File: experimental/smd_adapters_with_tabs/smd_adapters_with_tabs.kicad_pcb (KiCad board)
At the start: 2 copper layers, 79.8 x 64.6 mm, 34 parts

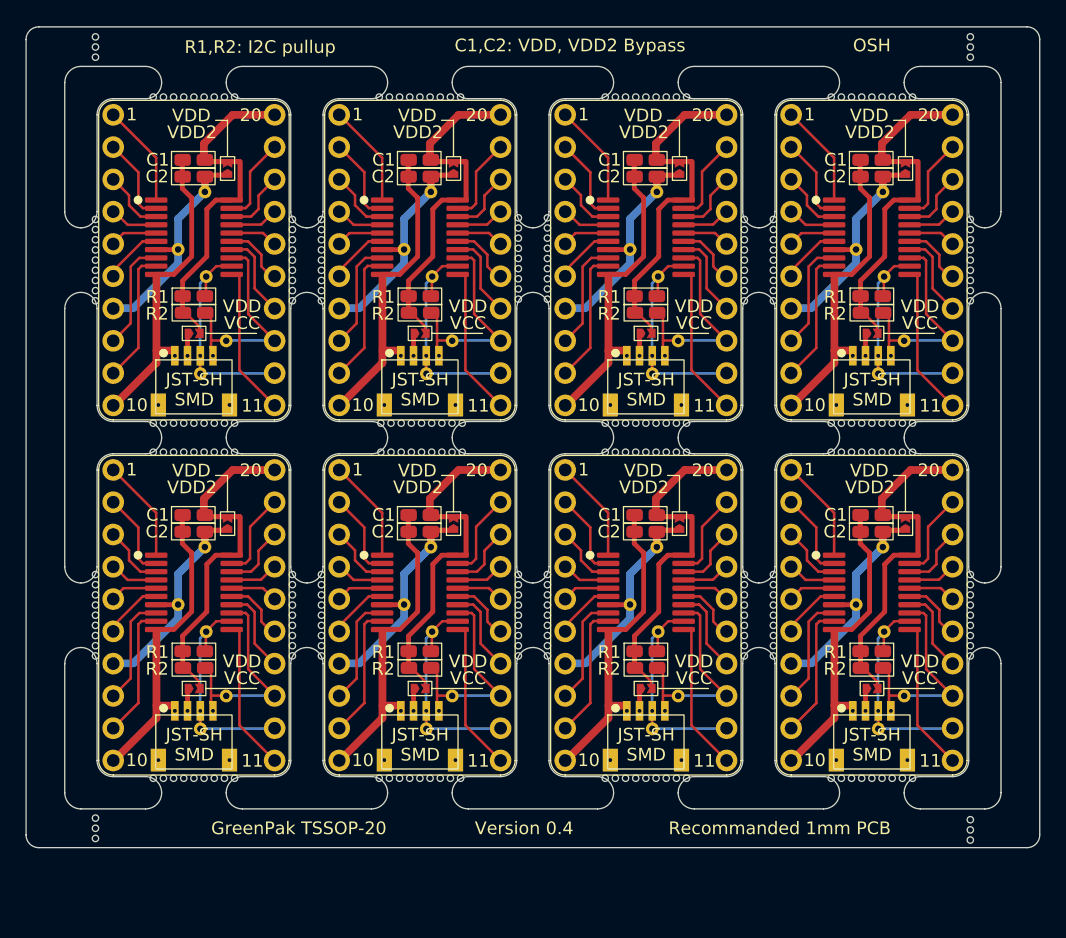
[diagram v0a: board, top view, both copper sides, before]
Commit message: Added the 24 pin footprints to the panel.
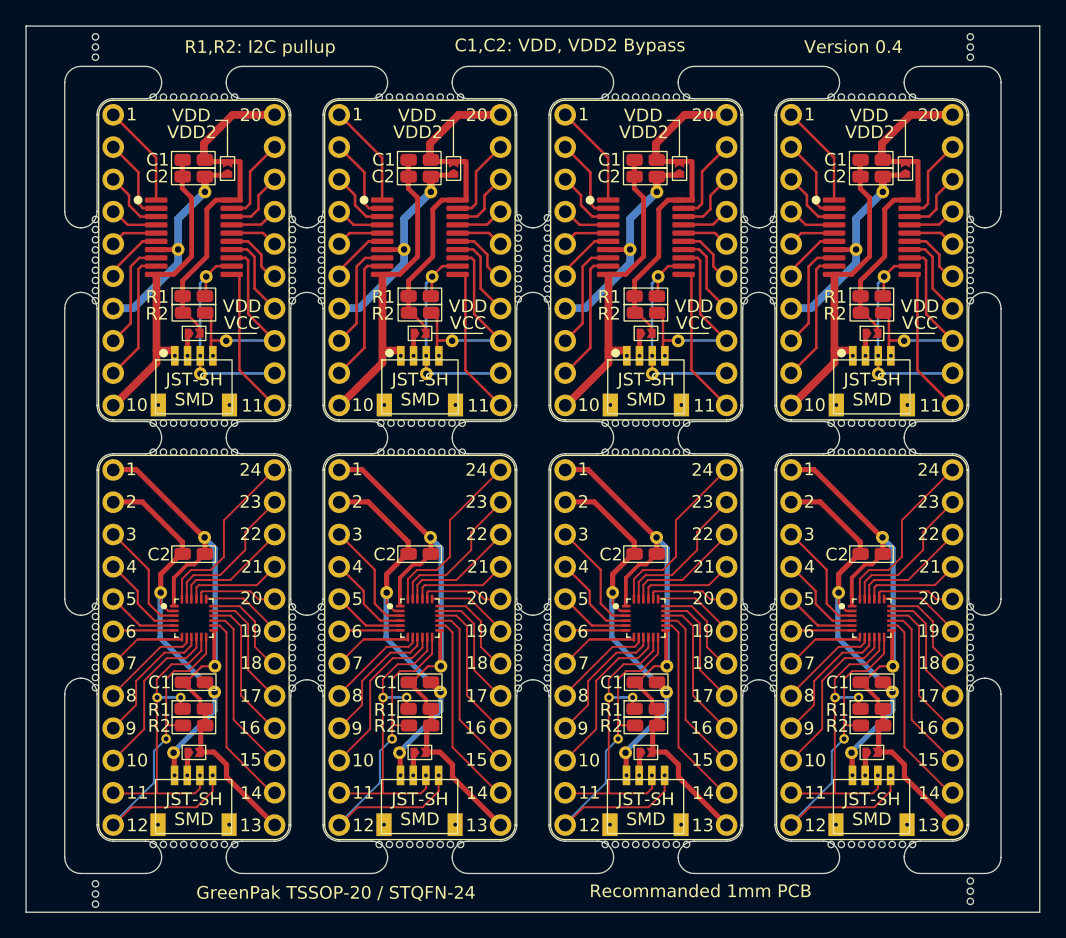
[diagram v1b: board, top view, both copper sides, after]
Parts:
- removed the REF** at (30.0, 6.86)
- removed the REF** at (-5.59, 6.86)
- removed the REF** at (-23.4, 6.86)
- removed the REF** at (12.2, 6.86)
- added REF**: GREENPAK-SMD-ADAPTER-STQFN-24-QWIIC, greenpack_smd_adapters:GREENPAK-SMD-ADAPTER-STQFN-24-QWIIC, F.Cu at (-5.59, 9.40)
- added REF**: GREENPAK-SMD-ADAPTER-STQFN-24-QWIIC, greenpack_smd_adapters:GREENPAK-SMD-ADAPTER-STQFN-24-QWIIC, F.Cu at (12.2, 9.40)
- added REF**: GREENPAK-SMD-ADAPTER-STQFN-24-QWIIC, greenpack_smd_adapters:GREENPAK-SMD-ADAPTER-STQFN-24-QWIIC, F.Cu at (-23.4, 9.40)
- added REF**: GREENPAK-SMD-ADAPTER-STQFN-24-QWIIC, greenpack_smd_adapters:GREENPAK-SMD-ADAPTER-STQFN-24-QWIIC, F.Cu at (30.0, 9.40)
- moved mouse-bite-2.54mm-slot 5.21 mm to (-5.59, 26.0)
- moved mouse-bite-2.54mm-slot 5.21 mm to (-23.4, 26.0)
- moved mouse-bite-2.54mm-slot 5.21 mm to (30.0, 26.0)
- moved mouse-bite-2.54mm-slot 5.21 mm to (12.2, 26.0)
- moved mouse-bite-2.54mm-slot 5.17 mm to (-32.3, 28.8)
- moved mouse-bite-2.54mm-slot 4.83 mm to (38.9, 28.6)
- moved mouse-bite-2.54mm-slot 2.54 mm to (21.1, 9.40)
- moved mouse-bite-2.54mm-slot 2.54 mm to (-14.5, 9.40)
- moved mouse-bite-2.54mm-slot 2.54 mm to (38.9, 9.40)
- moved mouse-bite-2.54mm-slot 2.54 mm to (3.30, 9.40)
- moved mouse-bite-2.54mm-slot 2.50 mm to (-32.3, 9.36)
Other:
- board size 79.8 x 64.6 mm -> 79.8 x 69.7 mm
- board text added: "GreenPak TSSOP-20 / STQFN-24"
- board text removed: "GreenPak TSSOP-20"
- board text removed: "OSH"

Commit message: Tweaked the SMD adapters
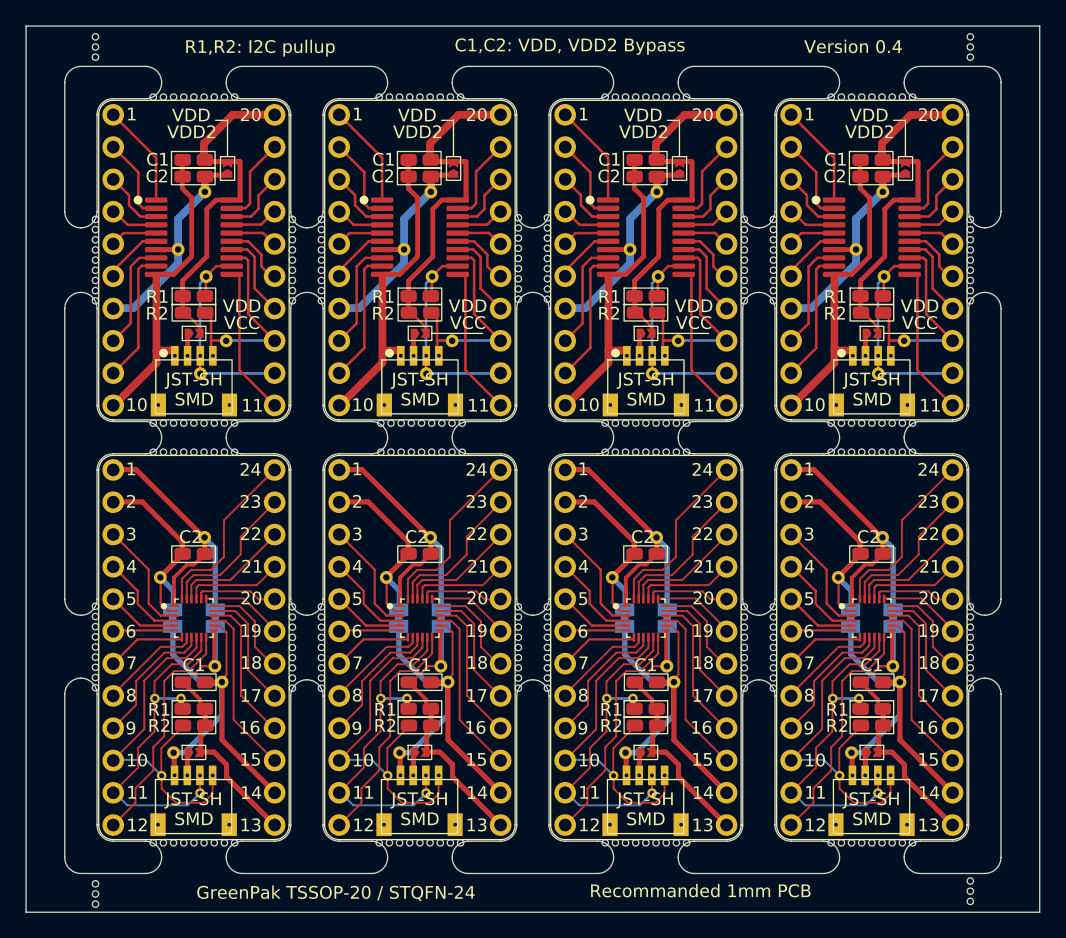
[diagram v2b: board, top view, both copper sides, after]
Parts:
- moved mouse-bite-2.54mm-slot 0.13 mm to (-5.59, 25.9)
- moved mouse-bite-2.54mm-slot 0.13 mm to (-23.4, 25.9)
- moved mouse-bite-2.54mm-slot 0.13 mm to (30.0, 25.9)
- moved mouse-bite-2.54mm-slot 0.13 mm to (12.2, 25.9)

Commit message: Deleted old greenak footprints
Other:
- board text removed: "C1: 0.1u 0603 (VDD bypass) C2: 0.1u 0603 (VDD2 bypass) R1: SDA pullup to VDD R2: SCL pullup to VDD2 Connector SH 1mm 4P horizontal (QWIIC) VDD2: Connects VDD and VDD2 VCC: Connects QWIIC VCC to VDD."
